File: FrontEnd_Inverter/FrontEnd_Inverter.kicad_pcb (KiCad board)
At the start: 4 copper layers, 215 x 126 mm, 82 parts, among them J11 CONN_02X06, P0 CONN_01X03, P1 CONN_01X03, P10 CONN_01X02, P11 CONN_01X03, P2 CONN_01X03, P20 CONN_01X02, P3 CONN_01X03, P4 CONN_01X03, P5 CONN_01X03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

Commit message: Further work on layout
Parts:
- removed the G*** at (226.2, 23.0)
- added G***: LOGO, Switchcraft:Switchcraft_logo_10px_stroke_200dpi, F.Cu at (183.7, 24.7)
- added REF**: MountingHole_3.2mm_M3_DIN965_Pad, MountingHole:MountingHole_3.2mm_M3_DIN965_Pad, F.Cu at (245.0, 19.0)
- added REF**: MountingHole_3.2mm_M3_DIN965_Pad, MountingHole:MountingHole_3.2mm_M3_DIN965_Pad, F.Cu at (245.0, 140.0)
- added REF**: MountingHole_3.2mm_M3_DIN965_Pad, MountingHole:MountingHole_3.2mm_M3_DIN965_Pad, F.Cu at (41.0, 140.0)
- added REF**: MountingHole_3.2mm_M3_DIN965_Pad, MountingHole:MountingHole_3.2mm_M3_DIN965_Pad, F.Cu at (41.0, 19.0)
- moved REF*** 8.00 mm to (237.4, 138.8)
- moved C5 3.37 mm to (130.6, 40.8)
- moved C22 3.09 mm to (188.1, 135.1)
- moved U40 3.09 mm to (170.0, 121.0)
- moved C7 3.09 mm to (145.3, 46.4)
- moved R7 3.09 mm to (145.3, 80.6)
- moved TP10 3.09 mm to (122.1, 73.2)
- moved C1 3.09 mm to (63.2, 48.9)
- moved C4 3.09 mm to (63.2, 110.0)
- moved C15 3.09 mm to (98.1, 126.5)
- moved C16 3.09 mm to (94.1, 123.3)
- moved C18 3.09 mm to (217.5, 118.6)
- moved C51 3.09 mm to (161.3, 109.7)
- moved C53 3.09 mm to (179.8, 112.6)
- moved D1 3.09 mm to (91.8, 79.9)
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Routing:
- net GND_ISO: track 155.2 -> 154.5 mm
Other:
- board size 215 x 126 mm -> 210 x 127 mm
- board text added: "13"
- board text added: "14"
- board text added: "Brake Chopper"
- board text added: "Brake Resistor"
- board text added: "DC Mid"
- board text added: "DC+"
- board text added: "DC-"
- board text added: "Inverter/Rectifier Combo Board"
- board text added: "L1"
- board text added: "L2"
- board text added: "L3"
- board text added: "Mains Supply"
- board text added: "Motor Connection"
- board text added: "Semikron SK 95 DGL 126"
- board text added: "Yngve was here"
- board text added: "c"
- board text added: "e"
- board text added: "g"
- board text added: "i+"
- board text added: "i-"
- board text added: "|-GND-|"
- board text removed: "11"
- board text removed: "12"
- board text removed: "Inverter/Rectifier Combo-Board"
- board text removed: "|—GND—|"

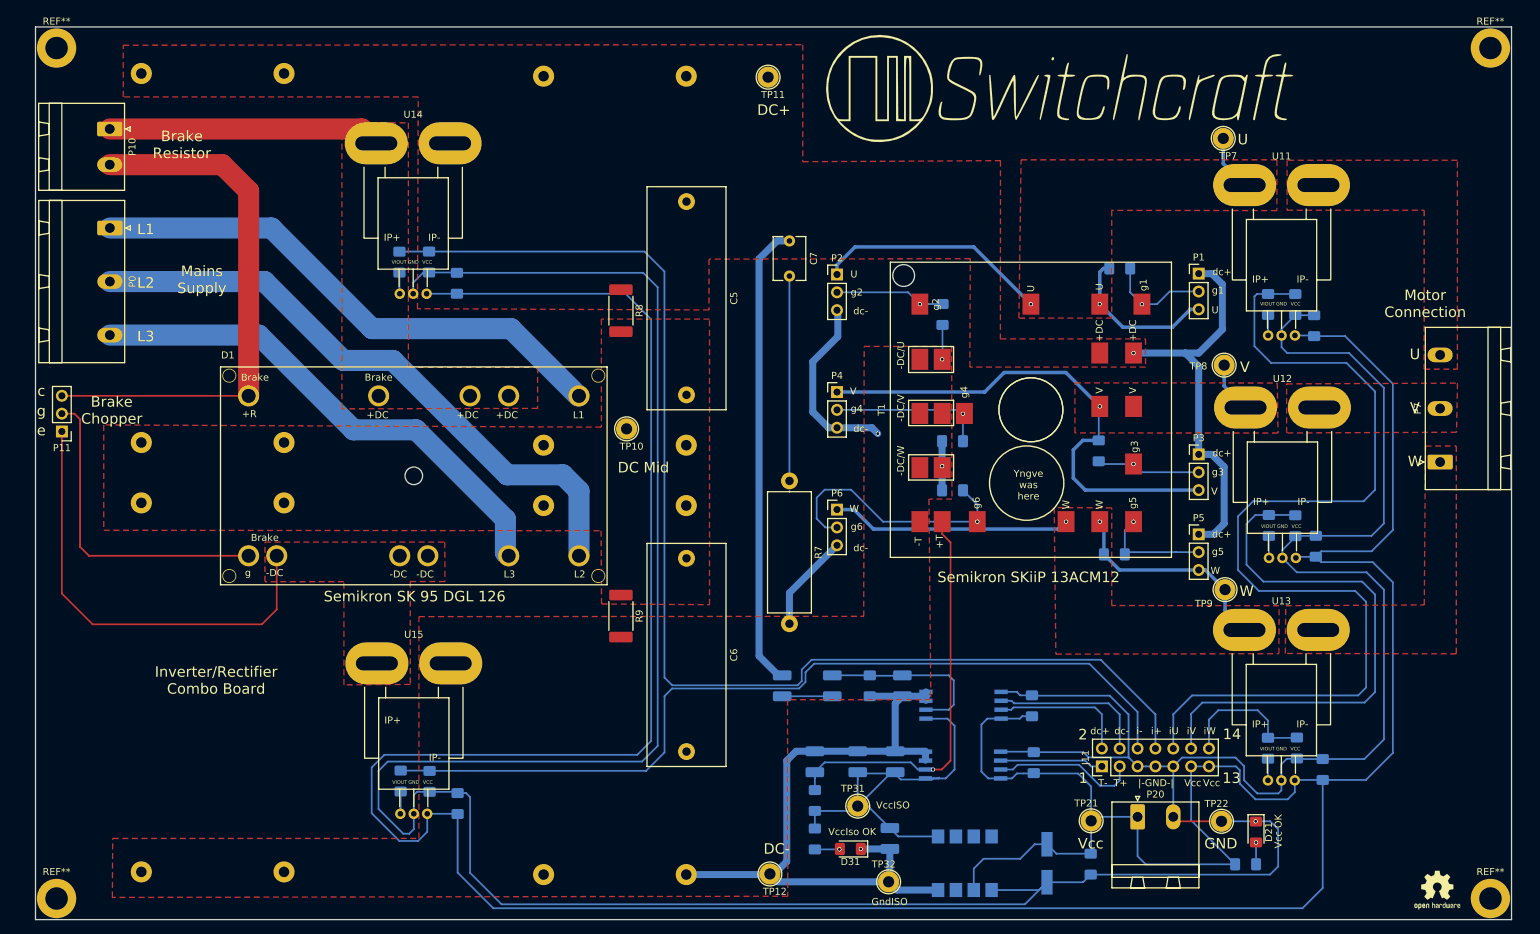
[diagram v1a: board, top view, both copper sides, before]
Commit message: Minor adjustments on tracks and traces.
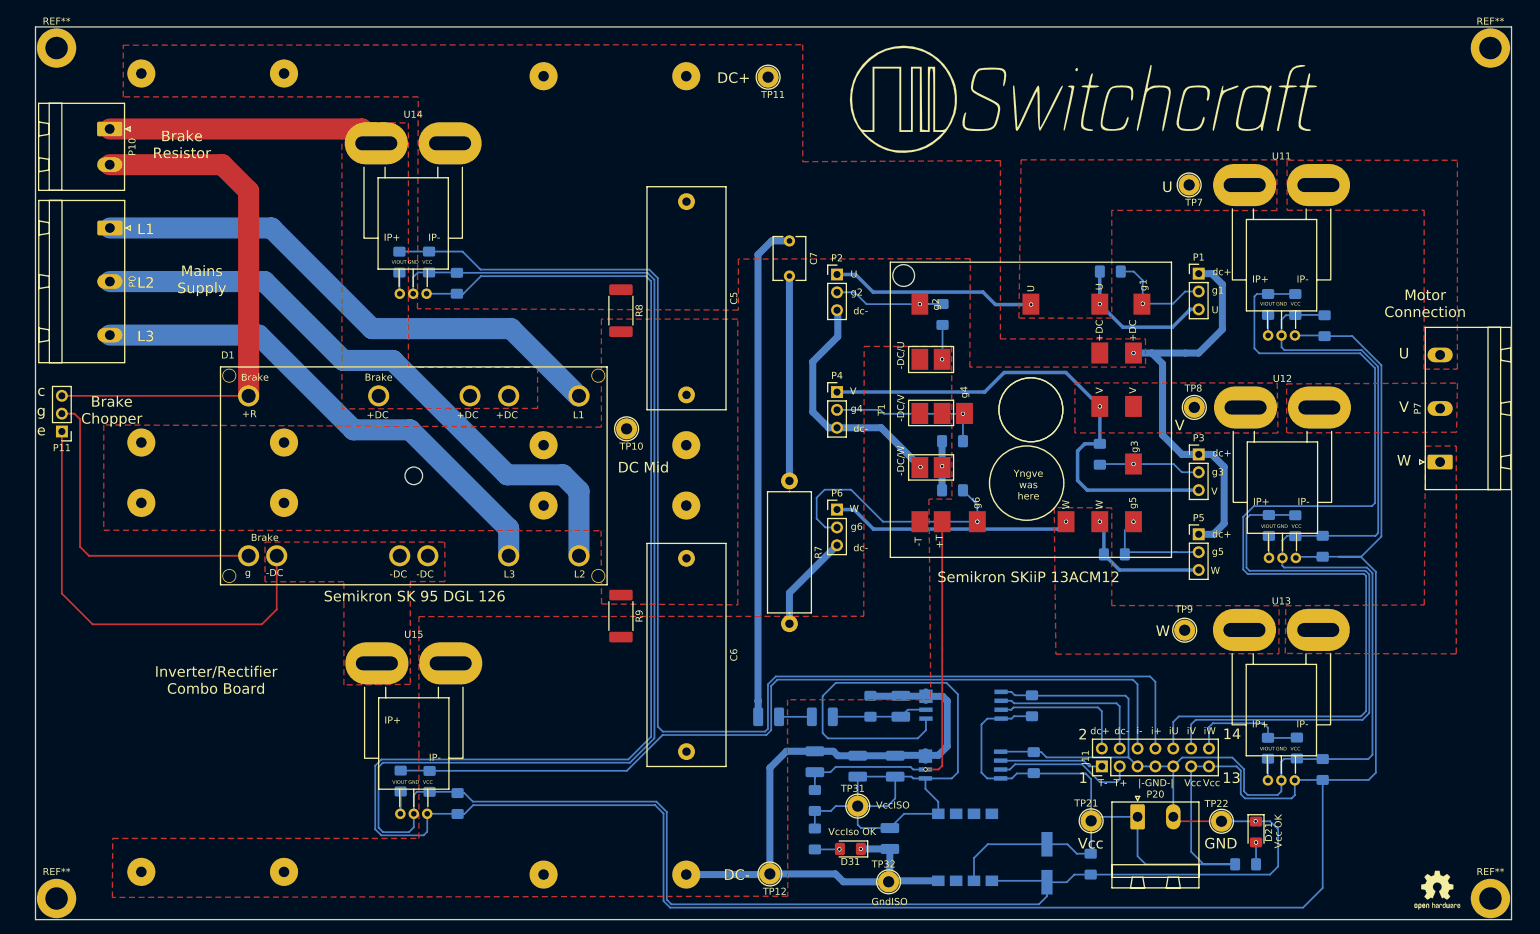
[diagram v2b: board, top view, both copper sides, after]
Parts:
- added G***: LOGO, Switchcraft:Switchcraft_logo_10px_stroke_200dpi, B.Cu at (192.6, 24.5)
- C1, C2, C3, C4: footprint Panasonic:Panasonic_EZPE80506MTA -> panasonic:Panasonic_EZPE80506MTA
- U30: footprint Package_DIP:SMDIP-8_W7.62mm -> Package_DIP:SMDIP-8_W9.53mm_Clearance8mm
- moved TP7 8.21 mm to (202.1, 38.5)
- moved TP9 8.14 mm to (201.5, 101.8)
- moved TP8 7.36 mm to (202.9, 70.1)
- moved R51 4.81 mm to (142.3, 114.1), turned to 0 degrees
- moved R52 4.63 mm to (149.9, 114.1), turned to 0 degrees
- moved G*** 3.73 mm to (187.1, 26.2)
- moved C51 2.92 mm to (161.1, 112.6), turned to 90 degrees
- moved R53 2.91 mm to (156.8, 112.6), turned to 90 degrees
- moved U30 2.27 mm to (170.3, 132.7)
- moved C11 1.49 mm to (221.4, 58.5)
- moved R1 1.41 mm to (190.9, 50.8)
- moved C12 0.98 mm to (221.1, 89.9)
- moved C42 0.64 mm to (155.0, 121.2)
- moved C52 0.64 mm to (160.3, 121.2)
- moved R3 0.52 mm to (189.4, 76.8)
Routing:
- net VCC_ISO: track 60.3 -> 112.2 mm
- net GND_ISO: track 154.5 -> 168.7 mm
- net U: track 63.9 -> 50.4 mm
- net Net-(C17-Pad1): track 177.5 -> 190.0 mm
- net W: track 65.4 -> 53.7 mm
- net Net-(C51-Pad1): track 25.0 -> 13.7 mm
- net GND: track 524.5 -> 533.8 mm
- net DC+: track 122.5 -> 130.6 mm
- net V: track 79.5 -> 71.7 mm
- net Net-(C20-Pad1): track 141.7 -> 146.9 mm
- net VCC: track 539.8 -> 544.2 mm
- net Net-(C18-Pad1): track 20.1 -> 17.3 mm
- net Net-(R51-Pad2): track 7.13 -> 4.67 mm
- net Net-(C41-Pad1): track 57.9 -> 56.1 mm
- net Net-(C19-Pad1): track 79.8 -> 81.4 mm
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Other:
- board text added: "Consider the environment before printing this circuit board"

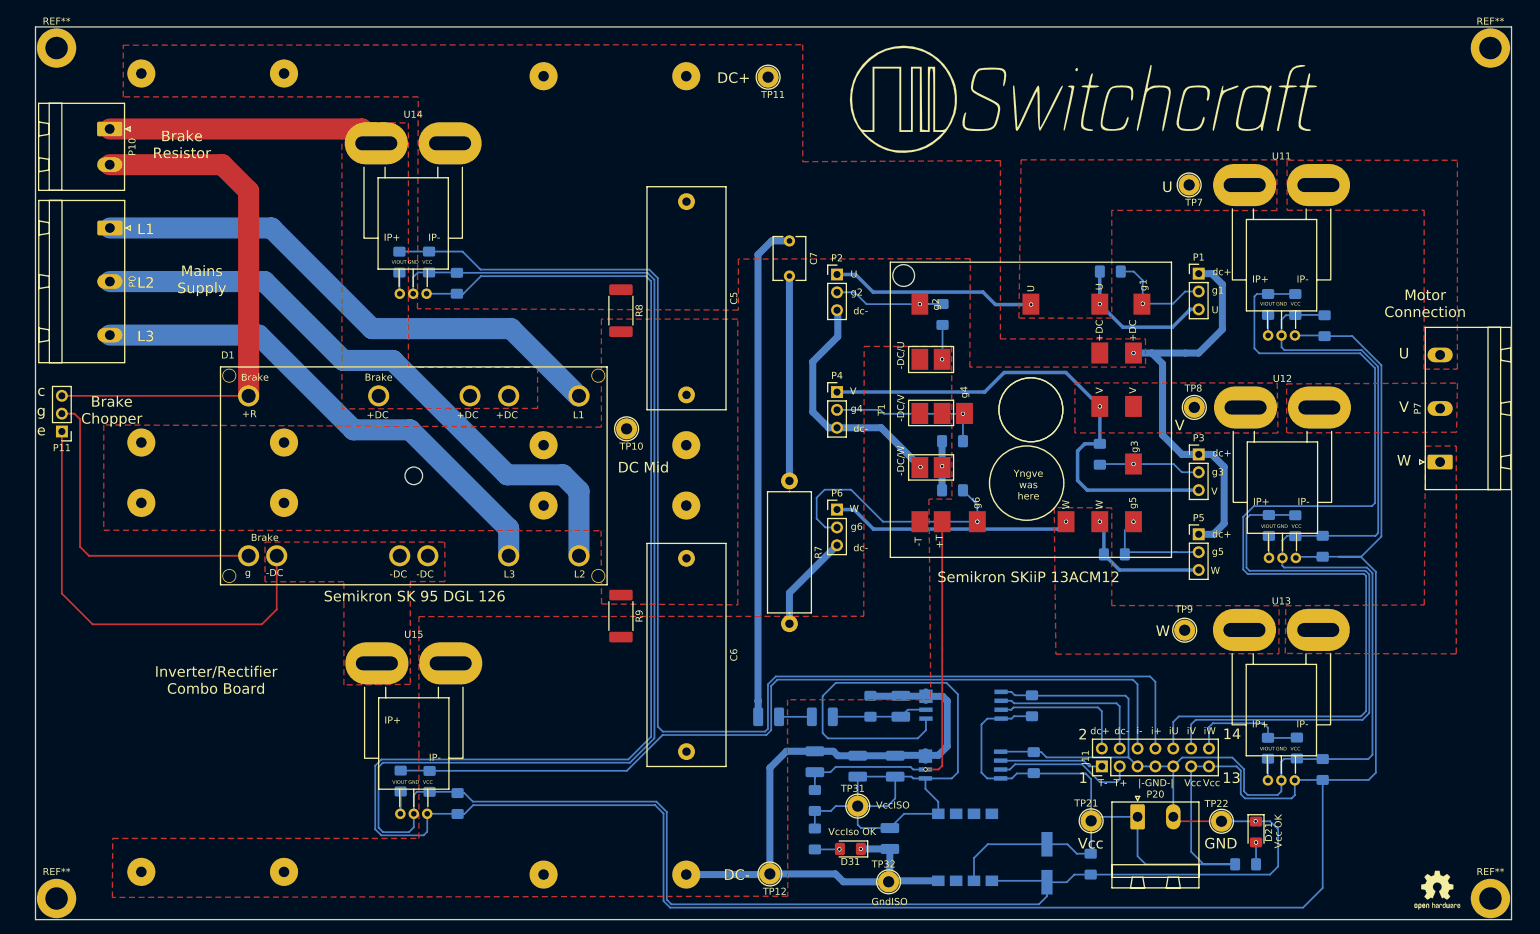
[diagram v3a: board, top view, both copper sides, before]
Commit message: Further work on pcb layout: new pinsocket + enlarged tracks for low voltage signals
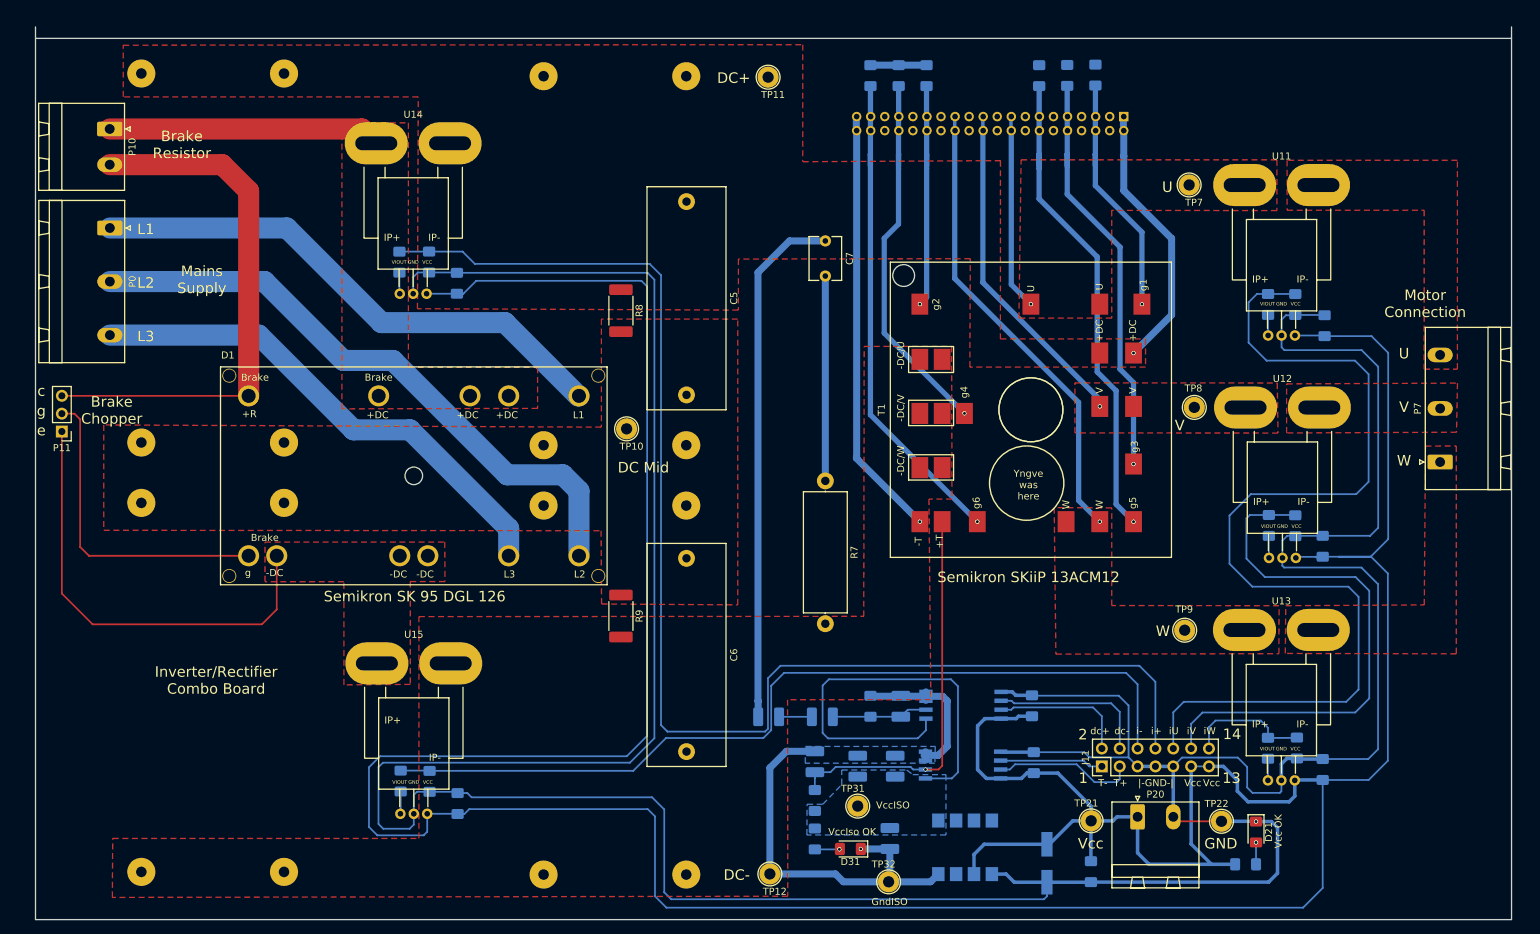
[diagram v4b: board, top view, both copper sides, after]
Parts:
- removed G*** (x2): LOGO, Switchcraft:Switchcraft_logo_10px_stroke_200dpi
- removed P1, P2, P3, P4, P5, P6: CONN_01X03, Connector_PinHeader_2.54mm:PinHeader_1x03_P2.54mm_Vertical
- removed REF** (x4): MountingHole_3.2mm_M3_DIN965_Pad, MountingHole:MountingHole_3.2mm_M3_DIN965_Pad
- removed REF***: OSHW-Logo2_7.3x6mm_SilkScreen, OpenSourceHardWare:OSHW-Logo2_7.3x6mm_SilkScreen
- added J1: Conn_02x20_Odd_Even, Connector_PinSocket_2.00mm:PinSocket_2x20_P2.00mm_Vertical, B.Cu at (192.8, 28.8)
- U30: footprint Package_DIP:SMDIP-8_W9.53mm_Clearance8mm -> Package_DIP:SMDIP-8_W7.62mm
- moved R5 69.0 mm to (180.8, 22.9), turned to 90 degrees
- moved R6 60.1 mm to (156.8, 22.9), turned to 90 degrees
- moved R3 54.1 mm to (184.8, 22.9)
- moved R4 52.6 mm to (160.8, 22.9), turned to 90 degrees
- moved R2 34.1 mm to (164.8, 22.9), turned to 90 degrees
- moved R1 28.0 mm to (188.8, 22.8), turned to 90 degrees
- moved C7 5.11 mm to (150.4, 46.4)
- moved R7 5.11 mm to (150.4, 80.6)
- moved C22 1.07 mm to (188.2, 136.2)
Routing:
- net T5_g: track 16.1 -> 69.2 mm
- net VCC_ISO: track 112.2 -> 61.5 mm
- net T3_g: track 14.9 -> 59.3 mm
- net T6_g: track 36.9 -> 69.9 mm
- net T4_g: track 22.0 -> 53.8 mm
- net V: track 71.7 -> 48.1 mm
- net U: track 50.4 -> 27.8 mm, vias 2 -> 1
- net T1_g: track 15.6 -> 35.5 mm
- net GND_ISO: track 168.7 -> 149.8 mm, vias 4 -> 2
- net T2_g: track 15.7 -> 33.1 mm
- net DC+: track 130.6 -> 113.4 mm
- net W: track 53.7 -> 66.2 mm, vias 2 -> 1
- net Net-(C20-Pad1): track 146.9 -> 142.1 mm
- net Net-(C19-Pad1): track 81.4 -> 78.1 mm
- net GND: track 533.8 -> 531.7 mm
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- added copper zone on B.Cu, net GND_ISO
- added copper zone on B.Cu, net VCC_ISO
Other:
- outline, holes or cut-outs redrawn
- net class Vcc_iso added: clearance 0.2, trace_width 0.5, via_dia 0.6, via_drill 0.4
- net class gates added: clearance 0.5, trace_width 0.75, via_dia 0.6, via_drill 0.4
- board text removed: "g1"
- board text removed: "g2"
- board text removed: "g3"
- board text removed: "g4"
- board text removed: "g5"
- board text removed: "g6"

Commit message: Further work on increasing zone area and track width
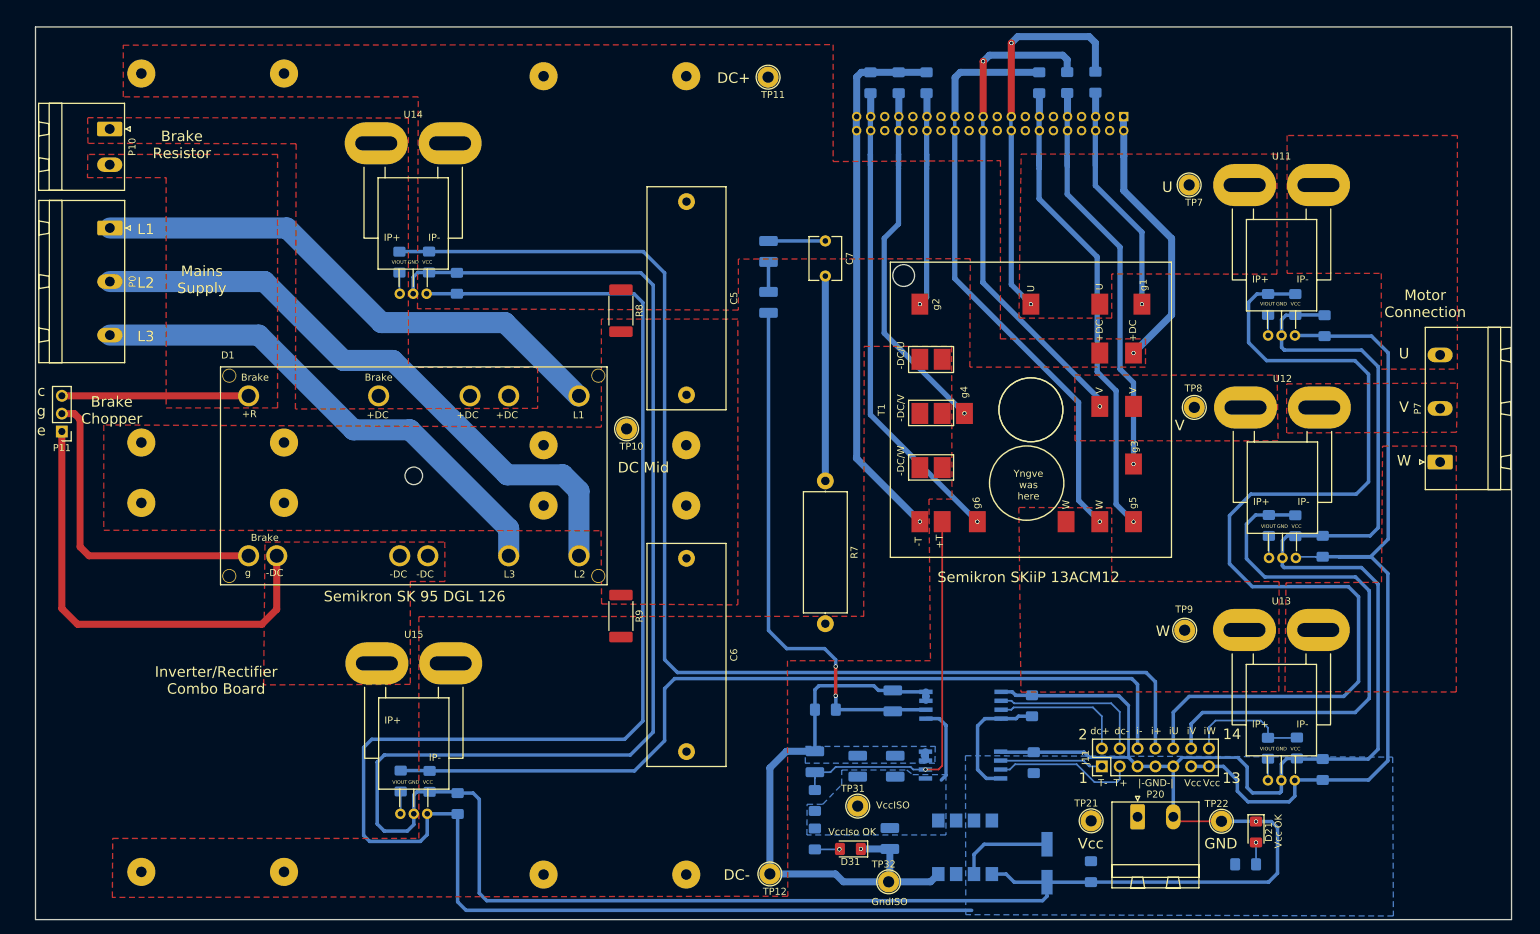
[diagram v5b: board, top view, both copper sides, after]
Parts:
- moved R51 66.2 mm to (142.3, 47.9), turned to 270 degrees
- moved R52 59.5 mm to (142.3, 55.2), turned to 270 degrees
- moved R53 6.43 mm to (150.4, 113.1), turned to 180 degrees
- moved C51 1.38 mm to (160.0, 111.9)
- moved R1 1.02 mm to (188.8, 23.9)
- moved R2 1.02 mm to (164.8, 23.9)
- moved R3 1.02 mm to (184.8, 23.9)
- moved R4 1.02 mm to (160.8, 23.9)
- moved R5 1.02 mm to (180.8, 23.9)
- moved R6 1.02 mm to (156.8, 23.9)
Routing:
- net VCC: track 542.9 -> 404.0 mm
- net DC+: track 113.4 -> 46.8 mm
- net Net-(C51-Pad1): track 13.7 -> 76.6 mm, vias 0 -> 2
- net Net-(D1-Pad14): track 77.0 -> 26.6 mm
- net VCC_ISO: track 61.5 -> 11.6 mm
- net Net-(D1-Pad4): track 38.8 -> 0.00 mm
- net U: track 27.8 -> 55.1 mm, vias 1 -> 2
- net V: track 48.1 -> 70.4 mm, vias 1 -> 2
- net W: track 66.2 -> 84.0 mm
- net Net-(C17-Pad1): track 191.9 -> 174.6 mm
- net GND_ISO: track 149.8 -> 161.5 mm
- net Net-(D1-Pad21): track 63.9 -> 65.2 mm
- net T3_g: track 59.3 -> 58.4 mm
- net T6_g: track 69.9 -> 69.0 mm
- net T5_g: track 69.2 -> 68.3 mm
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- added copper zone on F.Cu, net Net-(D1-Pad14)
- added copper zone on B.Cu, net VCC
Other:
- outline, holes or cut-outs redrawn
- board text added: "T1_g"
- board text added: "T2_g"
- board text added: "T3_g"
- board text added: "T4_g"
- board text added: "T5_g"
- board text added: "T6_g"
